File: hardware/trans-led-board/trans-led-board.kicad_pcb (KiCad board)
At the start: 2 copper layers, 12 x 33 mm, 4 parts, among them J1 Conn_01x02

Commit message: Updated properties, silkscreen, and page markings for Rev A
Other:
- board text added: "Rev: A 2021-06-15"
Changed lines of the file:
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@@
   (general
     (thickness 1.6)
-    (drawings 18)
+    (drawings 25)
     (tracks 10)
     (zones 0)
@@
   (title_block
     (title "Printalyzer Densitometer - Transmission LED Board")
-    (date 2021-06-??)
+    (date 2021-06-15)
     (rev A)
     (company LogicProbe.org)
@@
     (pad_to_paste_clearance_ratio -0.05)
     (aux_axis_origin 0 0)
-    (visible_elements FFFFFF7F)
+    (visible_elements FFFFFFFF)
     (pcbplotparams
       (layerselection 0x010fc_ffffffff)
@@
       (effects (font (size 1 1) (thickness 0.15)))
     )
+    (fp_line (start -2 -1.675) (end 2 -1.675) (layer F.Fab) (width 0.1))
+    (fp_line (start -2.11 0.715) (end -2.11 -1.785) (layer F.SilkS) (width 0.12))
+    (fp_line (start -2.11 -1.785) (end -1.06 -1.785) (layer F.SilkS) (width 0.12))
+    (fp_line (start -1.06 -1.785) (end -1.06 -2.775) (layer F.SilkS) (width 0.12))
+    (fp_line (start 2.11 0.715) (end 2.11 -1.785) (layer F.SilkS) (width 0.12))
+    (fp_line (start 2.11 -1.785) (end 1.06 -1.785) (layer F.SilkS) (width 0.12))
+    (fp_line (start -0.94 2.685) (end 0.94 2.685) (layer F.SilkS) (width 0.12))
+    (fp_line (start -2 2.575) (end 2 2.575) (layer F.Fab) (width 0.1))
+    (fp_line (start -2 -1.675) (end -2 2.575) (layer F.Fab) (width 0.1))
+    (fp_line (start 2 -1.675) (end 2 2.575) (layer F.Fab) (width 0.1))
+    (fp_line (start -2.9 -3.28) (end -2.9 3.28) (layer F.CrtYd) (width 0.05))
+    (fp_line (start -2.9 3.28) (end 2.9 3.28) (layer F.CrtYd) (width 0.05))
+    (fp_line (start 2.9 3.28) (end 2.9 -3.28) (layer F.CrtYd) (width 0.05))
+    (fp_line (start 2.9 -3.28) (end -2.9 -3.28) (layer F.CrtYd) (width 0.05))
+    (fp_line (start -1 -1.675) (end -0.5 -0.967893) (layer F.Fab) (width 0.1))
     (fp_line (start -0.5 -0.967893) (end 0 -1.675) (layer F.Fab) (width 0.1))
-    (fp_line (start -1 -1.675) (end -0.5 -0.967893) (layer F.Fab) (width 0.1))
-    (fp_line (start 2.9 -3.28) (end -2.9 -3.28) (layer F.CrtYd) (width 0.05))
-    (fp_line (start 2.9 3.28) (end 2.9 -3.28) (layer F.CrtYd) (width 0.05))
-    (fp_line (start -2.9 3.28) (end 2.9 3.28) (layer F.CrtYd) (width 0.05))
-    (fp_line (start -2.9 -3.28) (end -2.9 3.28) (layer F.CrtYd) (width 0.05))
-    (fp_line (start 2 -1.675) (end 2 2.575) (layer F.Fab) (width 0.1))
-    (fp_line (start -2 -1.675) (end -2 2.575) (layer F.Fab) (width 0.1))
-    (fp_line (start -2 2.575) (end 2 2.575) (layer F.Fab) (width 0.1))
-    (fp_line (start -0.94 2.685) (end 0.94 2.685) (layer F.SilkS) (width 0.12))
-    (fp_line (start 2.11 -1.785) (end 1.06 -1.785) (layer F.SilkS) (width 0.12))
-    (fp_line (start 2.11 0.715) (end 2.11 -1.785) (layer F.SilkS) (width 0.12))
-    (fp_line (start -1.06 -1.785) (end -1.06 -2.775) (layer F.SilkS) (width 0.12))
-    (fp_line (start -2.11 -1.785) (end -1.06 -1.785) (layer F.SilkS) (width 0.12))
-    (fp_line (start -2.11 0.715) (end -2.11 -1.785) (layer F.SilkS) (width 0.12))
-    (fp_line (start -2 -1.675) (end 2 -1.675) (layer F.Fab) (width 0.1))
     (fp_text user %R (at 0 0) (layer F.Fab)
       (effects (font (size 1 1) (thickness 0.15)))
@@
       (effects (font (size 1 1) (thickness 0.15)))
     )
+    (fp_line (start 1.6 -1.585) (end -2.285 -1.585) (layer F.SilkS) (width 0.12))
+    (fp_line (start -2.285 1.585) (end 1.6 1.585) (layer F.SilkS) (width 0.12))
+    (fp_line (start -2.285 -1.585) (end -2.285 1.585) (layer F.SilkS) (width 0.12))
+    (fp_line (start 2.28 1.58) (end -2.28 1.58) (layer F.CrtYd) (width 0.05))
+    (fp_line (start 2.28 -1.58) (end 2.28 1.58) (layer F.CrtYd) (width 0.05))
+    (fp_line (start -2.28 -1.58) (end 2.28 -1.58) (layer F.CrtYd) (width 0.05))
+    (fp_line (start -2.28 1.58) (end -2.28 -1.58) (layer F.CrtYd) (width 0.05))
+    (fp_line (start 1.6 1.25) (end 1.6 -1.25) (layer F.Fab) (width 0.1))
+    (fp_line (start -0.975 -1.25) (end -1.6 -0.625) (layer F.Fab) (width 0.1))
+    (fp_line (start 1.6 -1.25) (end -0.975 -1.25) (layer F.Fab) (width 0.1))
+    (fp_line (start -1.6 1.25) (end 1.6 1.25) (layer F.Fab) (width 0.1))
     (fp_line (start -1.6 -0.625) (end -1.6 1.25) (layer F.Fab) (width 0.1))
-    (fp_line (start -1.6 1.25) (end 1.6 1.25) (layer F.Fab) (width 0.1))
-    (fp_line (start 1.6 -1.25) (end -0.975 -1.25) (layer F.Fab) (width 0.1))
-    (fp_line (start -0.975 -1.25) (end -1.6 -0.625) (layer F.Fab) (width 0.1))
-    (fp_line (start 1.6 1.25) (end 1.6 -1.25) (layer F.Fab) (width 0.1))
-    (fp_line (start -2.28 1.58) (end -2.28 -1.58) (layer F.CrtYd) (width 0.05))
-    (fp_line (start -2.28 -1.58) (end 2.28 -1.58) (layer F.CrtYd) (width 0.05))
-    (fp_line (start 2.28 -1.58) (end 2.28 1.58) (layer F.CrtYd) (width 0.05))
-    (fp_line (start 2.28 1.58) (end -2.28 1.58) (layer F.CrtYd) (width 0.05))
-    (fp_line (start -2.285 -1.585) (end -2.285 1.585) (layer F.SilkS) (width 0.12))
-    (fp_line (start -2.285 1.585) (end 1.6 1.585) (layer F.SilkS) (width 0.12))
-    (fp_line (start 1.6 -1.585) (end -2.285 -1.585) (layer F.SilkS) (width 0.12))
     (fp_text user %R (at 0 0) (layer F.Fab)
       (effects (font (size 0.8 0.8) (thickness 0.12)))
@@
       (effects (font (size 1 1) (thickness 0.15)))
     )
+    (fp_circle (center 0 0) (end 2.2 0) (layer Cmts.User) (width 0.15))
     (fp_circle (center 0 0) (end 2.45 0) (layer F.CrtYd) (width 0.05))
-    (fp_circle (center 0 0) (end 2.2 0) (layer Cmts.User) (width 0.15))
     (fp_text user %R (at 0.3 0) (layer F.Fab)
       (effects (font (size 1 1) (thickness 0.15)))
@@
       (effects (font (size 1 1) (thickness 0.15)))
     )
+    (fp_circle (center 0 0) (end 2.2 0) (layer Cmts.User) (width 0.15))
     (fp_circle (center 0 0) (end 2.45 0) (layer F.CrtYd) (width 0.05))
-    (fp_circle (center 0 0) (end 2.2 0) (layer Cmts.User) (width 0.15))
     (fp_text user %R (at 0.3 0) (layer F.Fab)
       (effects (font (size 1 1) (thickness 0.15)))
@@
     (pad 1 np_thru_hole circle (at 0 0) (size 2.2 2.2) (drill 2.2) (layers *.Cu *.Mask))
   )
+  (gr_text "Rev: A\n2021-06-15" (at 124.079 75.565 90) (layer B.SilkS)
+    (effects (font (size 0.8128 0.8128) (thickness 0.1524)) (justify left mirror))
+  )
+  (gr_line (start 121.5 58) (end 122 58) (layer B.SilkS) (width 0.1524))
+  (gr_line (start 118 58) (end 118.5 58) (layer B.SilkS) (width 0.1524))
+  (gr_line (start 121.75 58.25) (end 121.75 57.75) (layer B.SilkS) (width 0.1524))
+  (gr_line (start 118 62.5) (end 118.5 62.5) (layer F.SilkS) (width 0.1524))
+  (gr_line (start 121.5 62.5) (end 122 62.5) (layer F.SilkS) (width 0.1524))
+  (gr_line (start 121.75 62.25) (end 121.75 62.75) (layer F.SilkS) (width 0.1524))
   (dimension 17.5 (width 0.15) (layer Cmts.User)
     (gr_text "17.500 mm" (at 134.3 81.25 90) (layer Cmts.User)

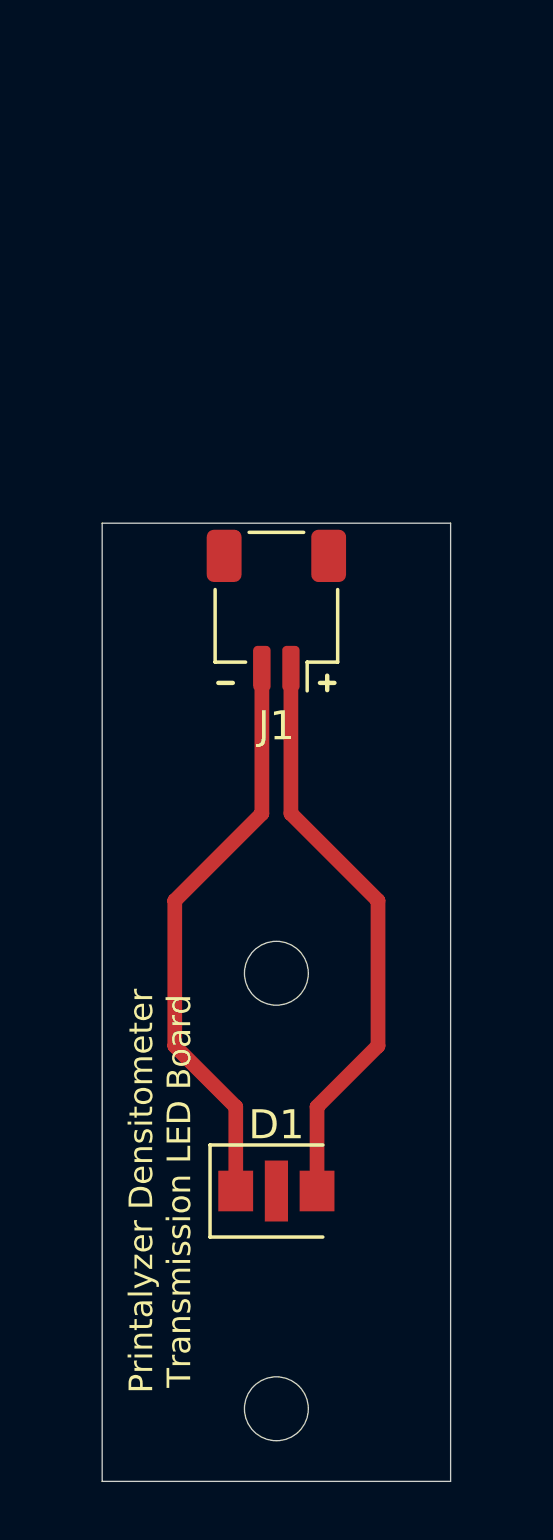
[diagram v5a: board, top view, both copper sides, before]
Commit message: Transmission LED board revision B update
This change is to test adding a substantial thermal pad around the LED,
to see if it has any measurable effect on the brightness drop.

If the test is successful, a similar footprint change will likely be
made to the main PCB for its next revision. If the test is unsuccessful,
this revision may simply be rolled back and forgotten about.
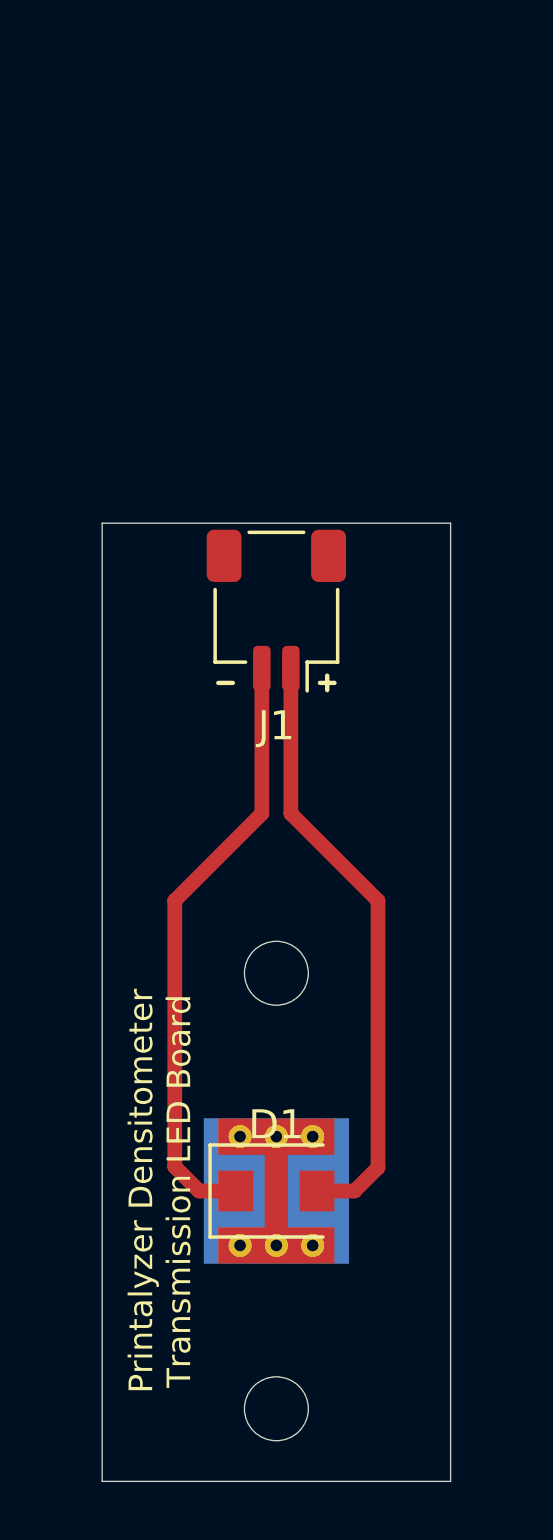
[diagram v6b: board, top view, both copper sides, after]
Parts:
- added LOGO: G1, lib_fp:Dektronics-logo, B.Cu at (124.1, 80.9)
- D1: footprint lib_fp:LED_WL-SWTP-3022 -> lib_fp:LED_WL-SWTP-3022-PAD
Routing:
- net Net-(D1-Pad2): track 20.1 -> 20.9 mm
- net Net-(D1-Pad1): track 20.1 -> 20.9 mm
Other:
- board text added: "Rev: B 2021-10-06"
- board text removed: "Rev: A 2021-06-15"

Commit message: Update LED footprints for thermal properties
Fixes naming convention of thermally-enhanced LED footprints to be
closer to the KiCad convention, and separates into two versions. One
with thermal vias and one without.

Updated transmission board metadata to referene the correct new
footprint name.

Updated main board to use the new version of the new footprint without
thermal vias.

Fixes #22
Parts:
- D1: footprint lib_fp:LED_WL-SWTP-3022-PAD -> lib_fp:LED_WL-SWTP-3022-1MP_ThermalVias
